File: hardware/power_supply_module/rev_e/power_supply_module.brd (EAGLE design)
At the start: 68.1 x 66 mm, 174 parts, among them J1 MODULE_POWER, J3 TC2030-FTDI-I2C, Q1 SSM6N7002KFU, U1 TLV62130, U10 LTC2943, U11 LTC2943, U12 LTC2943, U13 LTC2943, U14 LTC2943, U15 LTC2943, U16 LT3652, U17 LM234, U18 MAX17205, U19 ESDR0502N, U2 TLV62130, U20 AP22814, U21 AP22814, U22 AP22814, U23 AP22814, U24 AP22814, U25 PCA9544AQFN-N20, U26 LTC2943, U27 MAX6746, U28 3.3V, U29 M24C01WMN, U3 TLV62130, U4 TLV62130, U5 TLV62130, U6 PCA9544AQFN-N20, U7 PCA9544AQFN-N20, U8 LTC2941, U9 LTC2943

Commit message: a few nits
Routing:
- net GND: vias 90 -> 87
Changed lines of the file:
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@@
 <element name="C41" library="passives" package="0603_CAP" value="22 uF" x="17.526" y="12.573" smashed="yes" rot="R90">
 <attribute name="DIGIKEY" value="1276-1193-1-ND " x="17.526" y="12.573" size="1.778" layer="27" rot="R90" display="off"/>
-<attribute name="NAME" x="18.415" y="13.335" size="1.016" layer="25" font="vector" ratio="12" rot="R270" align="bottom-center"/>
+<attribute name="NAME" x="18.415" y="12.827" size="1.016" layer="25" font="vector" ratio="12" rot="R270" align="bottom-center"/>
 </element>
 <element name="R63" library="passives" package="0402_RES" value="750 kΩ" x="11.938" y="14.732" smashed="yes" rot="R180">
@@
 <element name="C46" library="passives" package="0603_CAP" value="22 uF" x="22.352" y="19.05" smashed="yes" rot="R270">
 <attribute name="DIGIKEY" value="1276-1193-1-ND " x="22.352" y="19.05" size="1.778" layer="27" rot="R270" display="off"/>
-<attribute name="NAME" x="23.622" y="20.32" size="1.016" layer="25" font="vector" ratio="12" align="bottom-center"/>
+<attribute name="NAME" x="24.13" y="20.32" size="1.016" layer="25" font="vector" ratio="12" rot="R90" align="bottom-center"/>
 </element>
 <element name="C15" library="passives" package="0402_CAP" value="0.1 uF" x="21.082" y="19.05" smashed="yes" rot="R90">
@@
 <element name="C21" library="passives" package="0402_CAP" value="0.1 uF" x="13.208" y="36.576" smashed="yes" rot="R90">
 <attribute name="DIGIKEY" value="490-5920-1-ND " x="13.208" y="36.576" size="1.778" layer="27" rot="R90" display="off"/>
-<attribute name="NAME" x="13.208" y="37.719" size="1.016" layer="25" font="vector" ratio="12" align="bottom-center"/>
+<attribute name="NAME" x="13.716" y="36.576" size="1.016" layer="25" font="vector" ratio="12" rot="R270" align="bottom-center"/>
 </element>
 <element name="C22" library="passives" package="0402_CAP" value="0.1 uF" x="12.192" y="33.782" smashed="yes">
@@
 <element name="R14" library="passives" package="0402_RES" value="1 MΩ" x="12.954" y="39.624" smashed="yes" rot="R90">
 <attribute name="DIGIKEY" value="P1.00MLCT-ND" x="12.954" y="39.624" size="1.778" layer="27" rot="R90" display="off"/>
-<attribute name="NAME" x="13.462" y="41.91" size="1.016" layer="25" font="vector" ratio="12" rot="R90" align="bottom-center"/>
+<attribute name="NAME" x="14.986" y="39.116" size="1.016" layer="25" font="vector" ratio="12" align="bottom-center"/>
 <attribute name="VALUE" x="14.351" y="39.624" size="1.016" layer="27" font="vector" ratio="12" rot="R90" align="bottom-center"/>
 </element>
@@
 <element name="R70" library="passives" package="0402_RES" value="150 Ω" x="11.684" y="39.624" smashed="yes" rot="R270">
 <attribute name="DIGIKEY" value="P150LCT-ND" x="11.684" y="39.624" size="1.778" layer="27" rot="R270" display="off"/>
-<attribute name="NAME" x="11.303" y="41.91" size="1.016" layer="25" font="vector" ratio="12" rot="R270" align="bottom-center"/>
+<attribute name="NAME" x="12.7" y="40.513" size="1.016" layer="25" font="vector" ratio="12" align="bottom-center"/>
 <attribute name="VALUE" x="10.287" y="39.624" size="1.016" layer="27" font="vector" ratio="12" rot="R270" align="bottom-center"/>
 </element>
@@
 <via x="26.67" y="44.45" extent="1-16" drill="0.254"/>
 <via x="19.304" y="47.752" extent="1-16" drill="0.254"/>
-<via x="18.542" y="19.812" extent="1-16" drill="0.254"/>
+<via x="16.764" y="19.558" extent="1-16" drill="0.254"/>
 <wire x1="53.844" y1="8.886" x2="54.102" y2="9.144" width="0.254" layer="1"/>
 <wire x1="53.344" y1="8.222" x2="53.344" y2="7.616" width="0.254" layer="1"/>
@@
 <wire x1="41.525" y1="19.308" x2="41.529" y2="19.304" width="0.254" layer="1"/>
 <via x="37.973" y="45.085" extent="1-16" drill="0.254"/>
-<via x="23.622" y="19.812" extent="1-16" drill="0.254"/>
 <contactref element="J3" pad="3"/>
 <wire x1="13.048" y1="11.18" x2="12.45" y2="11.18" width="0.3048" layer="1"/>
@@
 <via x="18.288" y="40.386" extent="1-16" drill="0.254"/>
 <via x="22.606" y="29.464" extent="1-16" drill="0.254"/>
-<via x="22.098" y="21.336" extent="1-16" drill="0.254"/>
-<via x="9.144" y="38.1" extent="1-16" drill="0.254"/>
-<via x="19.304" y="21.336" extent="1-16" drill="0.254"/>
-<via x="24.638" y="21.336" extent="1-16" drill="0.254"/>
+<via x="12.192" y="38.1" extent="1-16" drill="0.254"/>
+<via x="25.146" y="21.844" extent="1-16" drill="0.254"/>
 <via x="26.67" y="34.544" extent="1-16" drill="0.254"/>
 <via x="16.51" y="41.148" extent="1-16" drill="0.254"/>
@@
 <contactref element="Q1" pad="3"/>
 <wire x1="10.502" y1="41.798" x2="10.502" y2="42.506" width="0.254" layer="1"/>
-<wire x1="10.502" y1="42.506" x2="11.43" y2="43.434" width="0.254" layer="1"/>
-<via x="11.43" y="43.434" extent="1-16" drill="0.254"/>
-<wire x1="11.43" y1="43.434" x2="16.764" y2="43.434" width="0.254" layer="15"/>
-<wire x1="16.764" y1="43.434" x2="17.272" y2="42.926" width="0.254" layer="15"/>
-<wire x1="17.272" y1="42.926" x2="23.876" y2="42.926" width="0.254" layer="15"/>
+<wire x1="10.502" y1="42.506" x2="10.922" y2="42.926" width="0.254" layer="1"/>
+<via x="10.922" y="42.926" extent="1-16" drill="0.254"/>
 <wire x1="23.876" y1="42.926" x2="26.67" y2="45.72" width="0.254" layer="15"/>
+<wire x1="10.922" y1="42.926" x2="23.876" y2="42.926" width="0.254" layer="15"/>
 </signal>
 <signal name="VCC_5V_1">

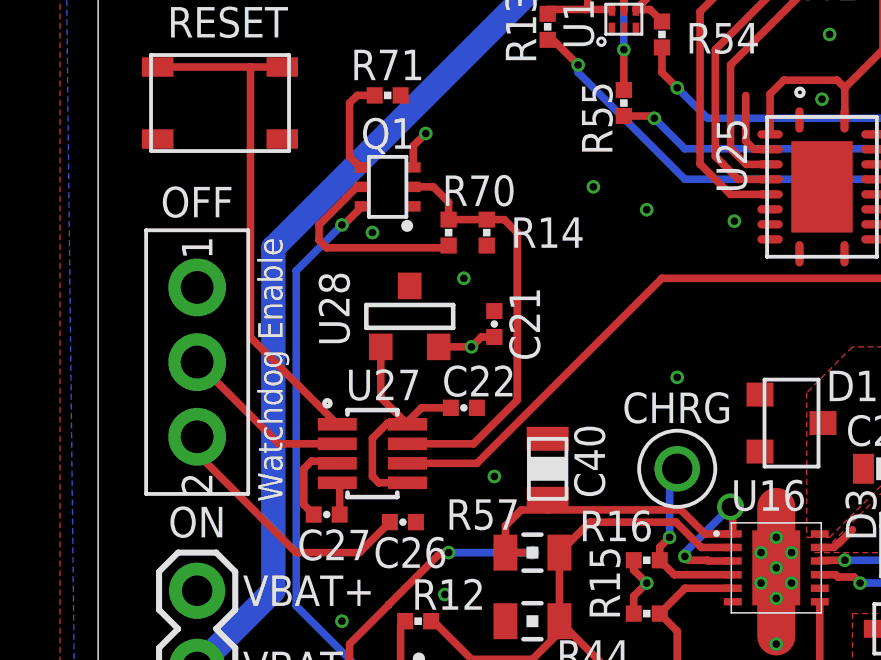
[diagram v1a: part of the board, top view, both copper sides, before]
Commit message: Generate gerbers and bom
Made small changes to brd
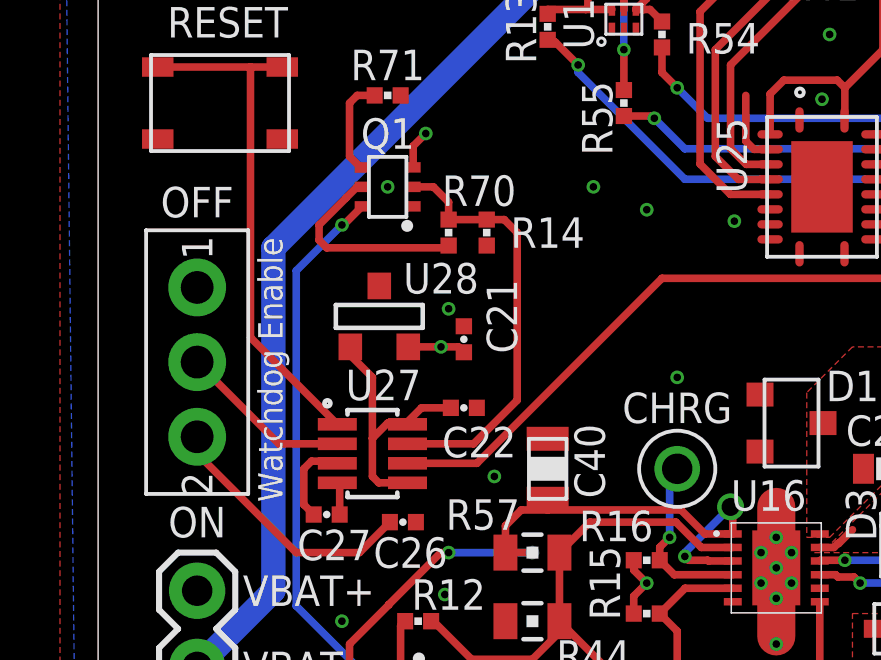
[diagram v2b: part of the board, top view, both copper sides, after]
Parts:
- moved C21 1.14 mm to (12.2, 36.1)
- moved U28 1.02 mm to (9.40, 36.8)
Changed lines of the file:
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@@
 <attribute name="NAME" x="7.874" y="29.718" size="1.016" layer="25" font="vector" ratio="12" rot="R180" align="bottom-center"/>
 </element>
-<element name="U28" library="chips" package="SOT-23" value="3.3V" x="10.414" y="36.83" smashed="yes" rot="R180">
-<attribute name="DIGIKEY" value="ZMR330FCT-ND" x="30.734" y="3.81" size="1.778" layer="27" font="vector" ratio="12" rot="R180" display="off"/>
-<attribute name="NAME" x="8.382" y="37.084" size="1.016" layer="25" font="vector" ratio="12" rot="R90" align="bottom-center"/>
-<attribute name="VALUE" x="10.414" y="39.37" size="1.016" layer="27" font="vector" ratio="12" rot="R180" align="bottom-center"/>
+<element name="U28" library="chips" package="SOT-23" value="3.3V" x="9.398" y="36.83" smashed="yes" rot="R180">
+<attribute name="DIGIKEY" value="ZMR330FCT-ND" x="29.718" y="3.81" size="1.778" layer="27" font="vector" ratio="12" rot="R180" display="off"/>
+<attribute name="NAME" x="11.43" y="37.592" size="1.016" layer="25" font="vector" ratio="12" align="bottom-center"/>
+<attribute name="VALUE" x="9.398" y="39.37" size="1.016" layer="27" font="vector" ratio="12" rot="R180" align="bottom-center"/>
 </element>
-<element name="C21" library="passives" package="0402_CAP" value="0.1 uF" x="13.208" y="36.576" smashed="yes" rot="R90">
-<attribute name="DIGIKEY" value="490-5920-1-ND " x="13.208" y="36.576" size="1.778" layer="27" rot="R90" display="off"/>
-<attribute name="NAME" x="13.716" y="36.576" size="1.016" layer="25" font="vector" ratio="12" rot="R270" align="bottom-center"/>
+<element name="C21" library="passives" package="0402_CAP" value="0.1 uF" x="12.192" y="36.068" smashed="yes" rot="R90">
+<attribute name="DIGIKEY" value="490-5920-1-ND " x="12.192" y="36.068" size="1.778" layer="27" rot="R90" display="off"/>
+<attribute name="NAME" x="12.954" y="36.83" size="1.016" layer="25" font="vector" ratio="12" rot="R270" align="bottom-center"/>
 </element>
 <element name="C22" library="passives" package="0402_CAP" value="0.1 uF" x="12.192" y="33.782" smashed="yes">
 <attribute name="DIGIKEY" value="490-5920-1-ND " x="12.192" y="33.782" size="1.778" layer="27" display="off"/>
-<attribute name="NAME" x="12.7" y="34.163" size="1.016" layer="25" font="vector" ratio="12" align="bottom-center"/>
+<attribute name="NAME" x="12.7" y="33.147" size="1.016" layer="25" font="vector" ratio="12" rot="R180" align="bottom-center"/>
 </element>
 <element name="R14" library="passives" package="0402_RES" value="1 MΩ" x="12.954" y="39.624" smashed="yes" rot="R90">
@@
 <via x="18.288" y="40.386" extent="1-16" drill="0.254"/>
 <via x="22.606" y="29.464" extent="1-16" drill="0.254"/>
-<via x="12.192" y="38.1" extent="1-16" drill="0.254"/>
+<via x="11.684" y="37.084" extent="1-16" drill="0.254"/>
 <via x="25.146" y="21.844" extent="1-16" drill="0.254"/>
 <via x="26.67" y="34.544" extent="1-16" drill="0.254"/>
@@
 <contactref element="U16" pad="6"/>
 <contactref element="C40" pad="P$2"/>
-<via x="9.144" y="39.624" extent="1-16" drill="0.254"/>
+<via x="9.652" y="41.148" extent="1-16" drill="0.254"/>
 <via x="13.208" y="31.496" extent="1-16" drill="0.254"/>
 <wire x1="17.78" y1="50.038" x2="17.526" y2="50.292" width="0.1524" layer="1"/>
@@
 <wire x1="8.255" y1="17.907" x2="8.128" y2="17.78" width="0.254" layer="1"/>
 <via x="8.128" y="17.78" extent="1-16" drill="0.254"/>
-<wire x1="11.3538" y1="35.814" x2="12.446" y2="35.814" width="0.254" layer="1"/>
-<wire x1="12.446" y1="35.814" x2="12.77493125" y2="36.14293125" width="0.254" layer="1"/>
-<wire x1="12.77493125" y1="36.14293125" x2="13.208" y2="36.14293125" width="0.254" layer="1"/>
-<via x="12.446" y="35.814" extent="1-16" drill="0.254"/>
+<via x="11.43" y="35.814" extent="1-16" drill="0.254"/>
+<wire x1="10.3378" y1="35.814" x2="11.43" y2="35.814" width="0.254" layer="1"/>
+<wire x1="11.43" y1="35.814" x2="12.01293125" y2="35.814" width="0.254" layer="1"/>
+<wire x1="12.01293125" y1="35.814" x2="12.192" y2="35.63493125" width="0.254" layer="1"/>
 </signal>
 <signal name="VCC_LINUX">
@@
 <wire x1="10.314" y1="31.283" x2="9.357" y2="31.283" width="0.254" layer="1"/>
 <wire x1="9.357" y1="31.283" x2="9.144" y2="31.496" width="0.254" layer="1"/>
-<wire x1="9.144" y1="31.496" x2="9.144" y2="32.766" width="0.254" layer="1"/>
+<wire x1="9.144" y1="32.766" x2="9.144" y2="31.496" width="0.254" layer="1"/>
 <wire x1="10.273" y1="33.274" x2="9.652" y2="33.274" width="0.254" layer="1"/>
 <wire x1="10.273" y1="33.274" x2="10.314" y2="33.233" width="0.254" layer="1"/>
 <wire x1="9.144" y1="32.766" x2="9.652" y2="33.274" width="0.254" layer="1"/>
-<wire x1="9.4234" y1="35.814" x2="9.4234" y2="34.1236" width="0.254" layer="1"/>
-<wire x1="9.4234" y1="34.1236" x2="10.273" y2="33.274" width="0.254" layer="1"/>
 <wire x1="11.75893125" y1="33.782" x2="10.781" y2="33.782" width="0.254" layer="1"/>
 <wire x1="10.781" y1="33.782" x2="10.273" y2="33.274" width="0.254" layer="1"/>
+<wire x1="8.4074" y1="35.814" x2="8.4074" y2="35.5346" width="0.254" layer="1"/>
+<wire x1="8.4074" y1="35.5346" x2="9.144" y2="34.798" width="0.254" layer="1"/>
+<wire x1="9.144" y1="34.798" x2="9.144" y2="32.766" width="0.254" layer="1"/>
 </signal>
 <signal name="N$45">
